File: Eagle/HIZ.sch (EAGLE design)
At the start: 17 parts, among them IC1 IC_UC_PIC12F508SOIC, SW1 SW_TACT_2P-3X6, SW2 SW_SLIDE

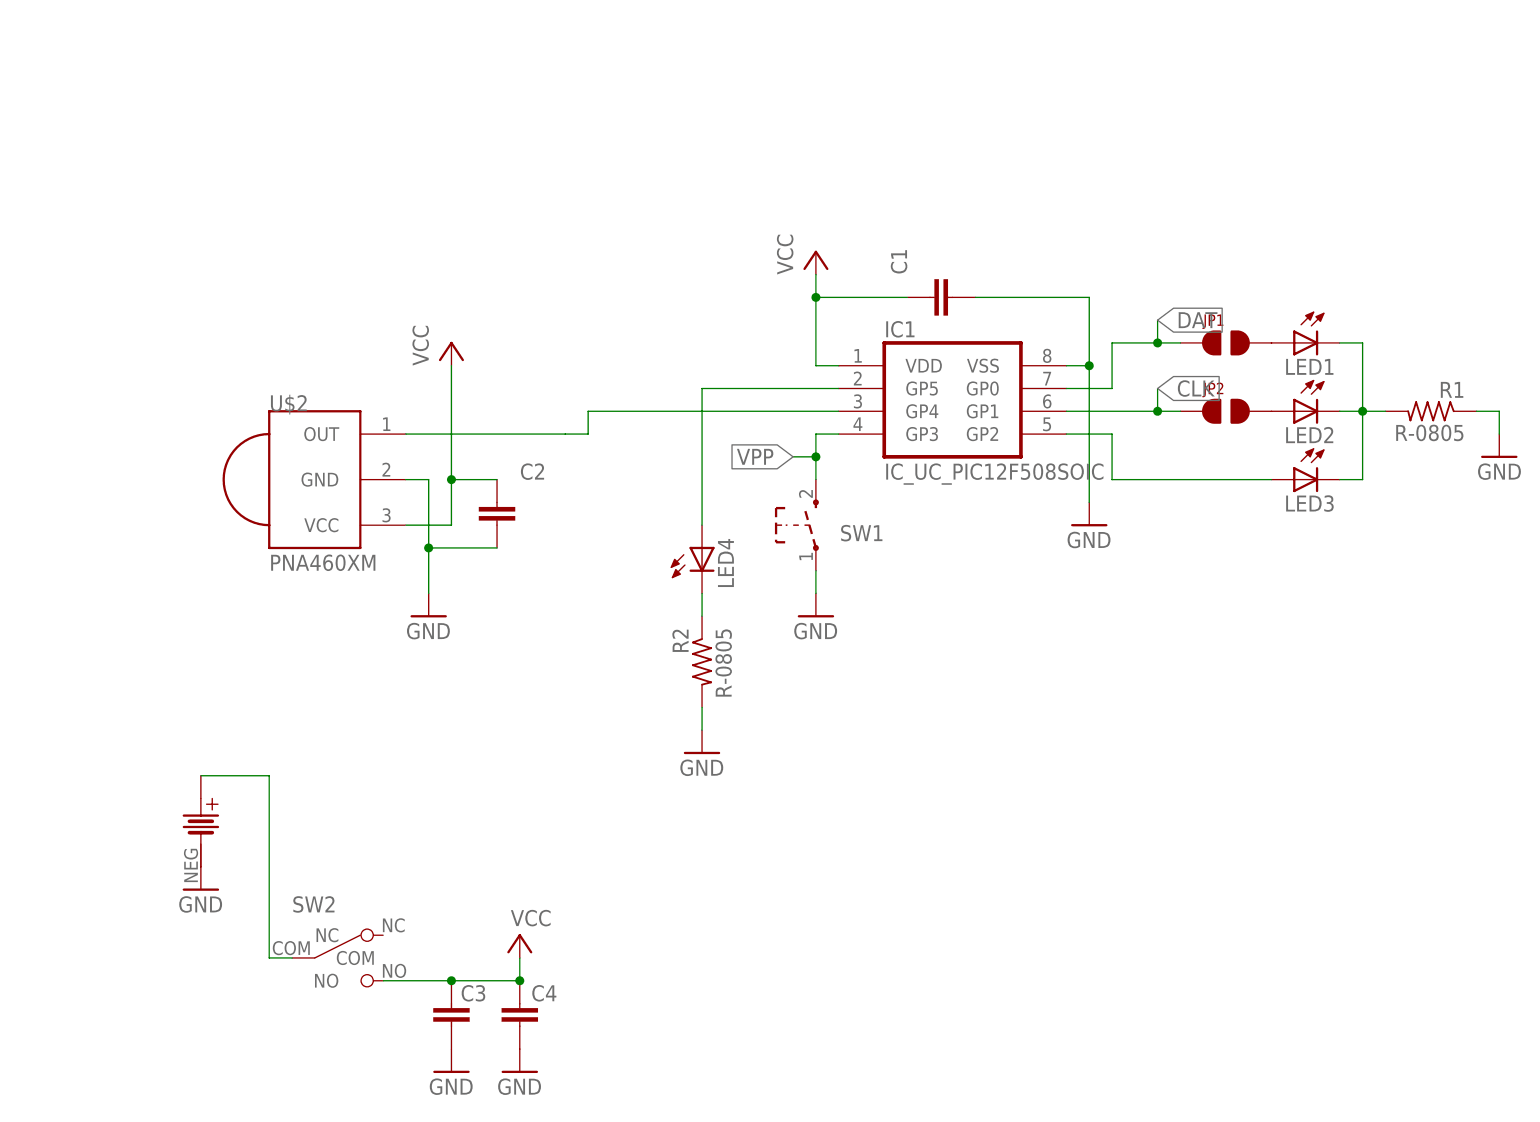
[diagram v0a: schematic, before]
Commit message: Added Frame to schematics
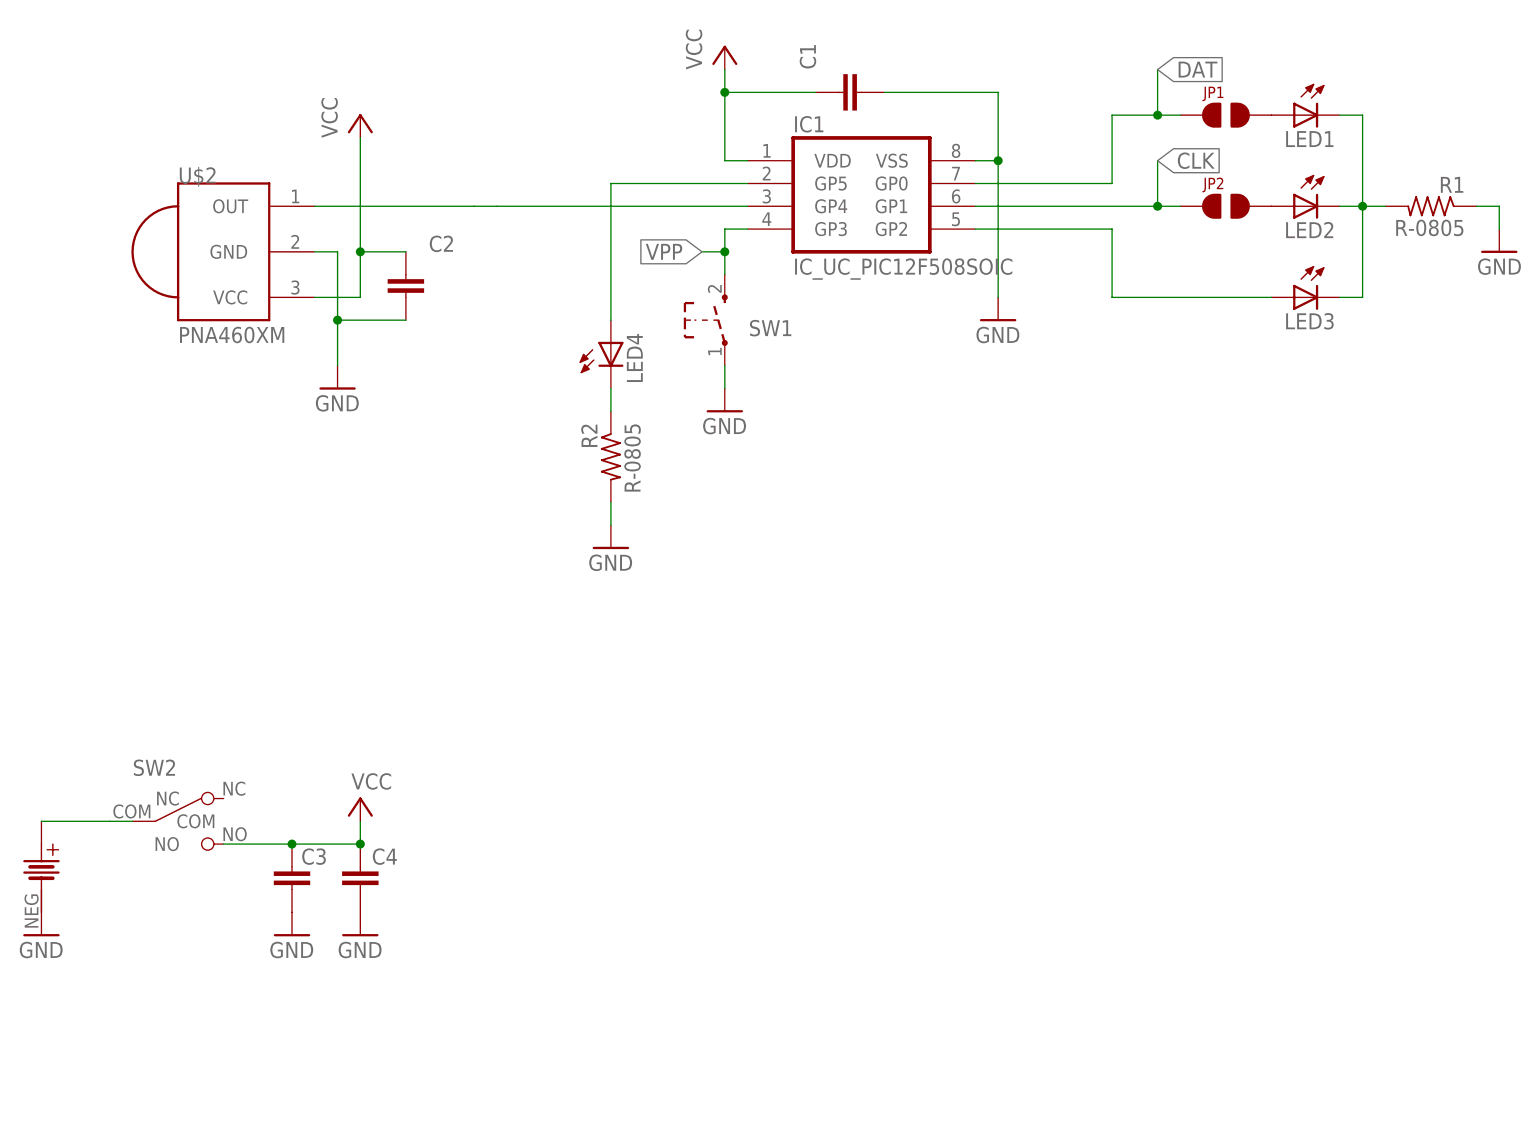
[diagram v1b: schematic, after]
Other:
- moved on the sheet: C1, C2, C3, C4, IC1, JP1, JP2, LED1, LED2, LED3, LED4, R1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

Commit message: Updated info in Frame, added part values.
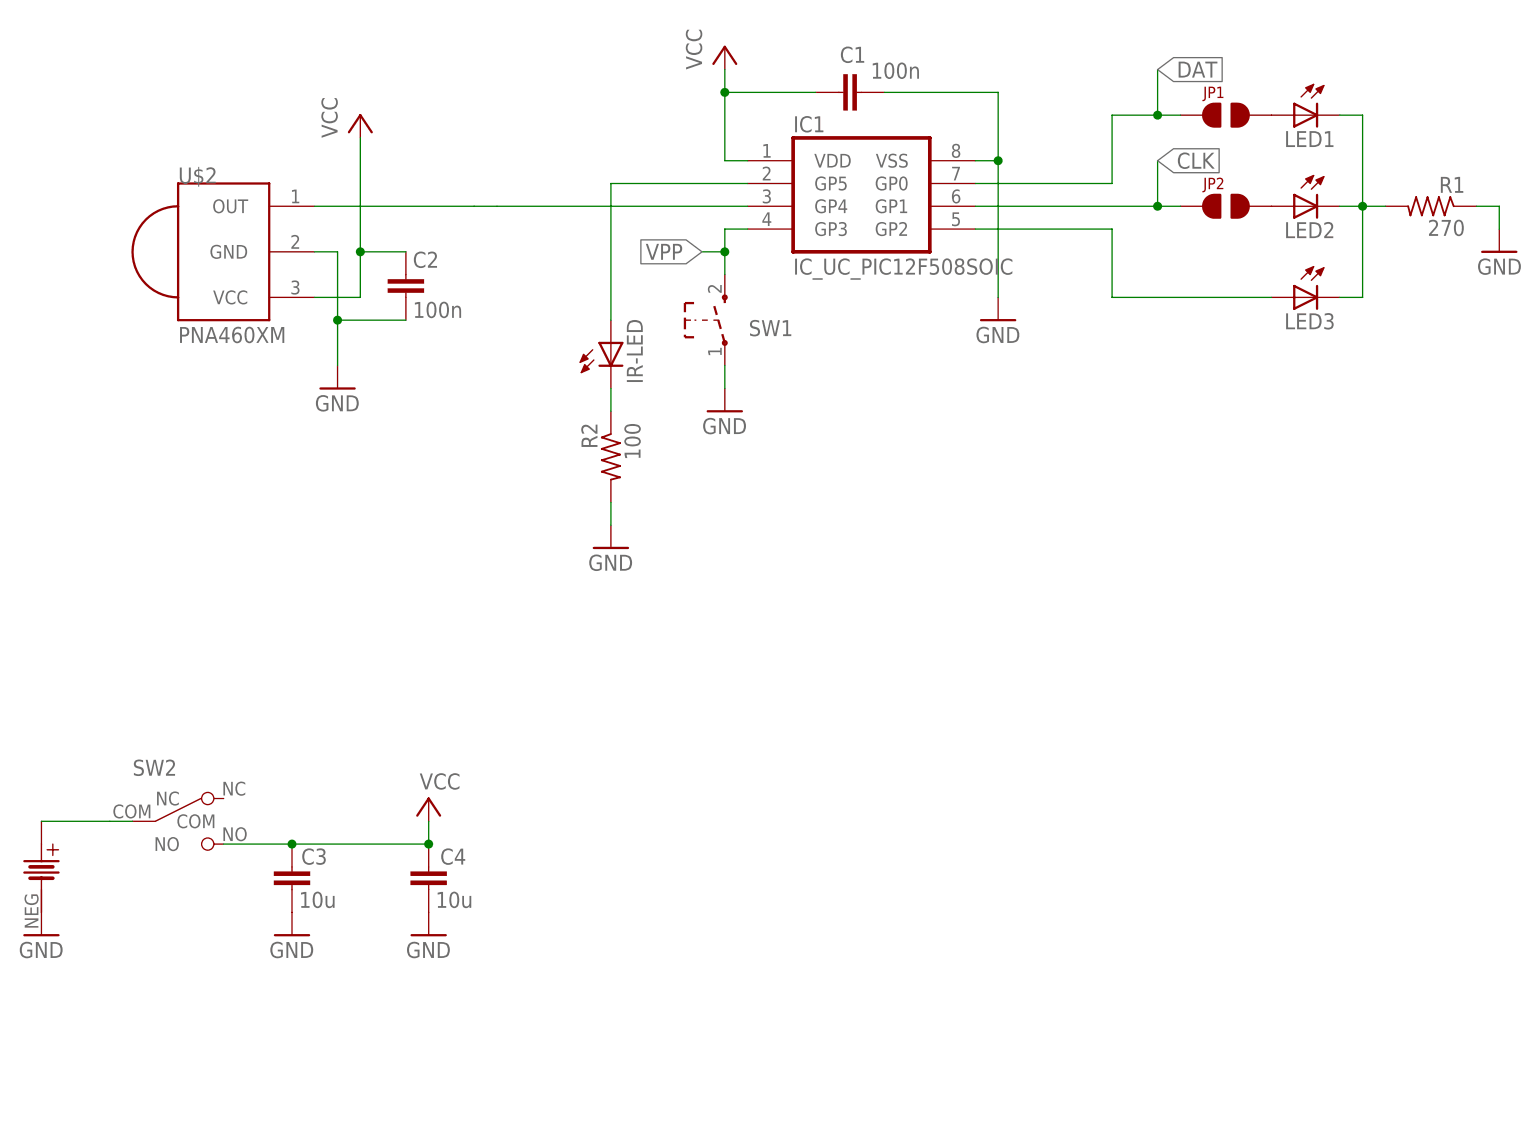
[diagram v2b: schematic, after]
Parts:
- C1, C2: value (none) -> 100n
- C3, C4: value (none) -> 10u
- R1: value R-0805 -> 270
- R2: value R-0805 -> 100
- renumbered LED4 to IR-LED
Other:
- moved on the sheet: C4
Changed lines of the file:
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@@
 <part name="LED2" library="dp_devices" deviceset="LED" device="-0805"/>
 <part name="LED3" library="dp_devices" deviceset="LED" device="-0805"/>
-<part name="LED4" library="adafruit" deviceset="LED" device="SMT1206"/>
+<part name="IR-LED" library="adafruit" deviceset="LED" device="SMT1206"/>
 <part name="SW1" library="dp_devices" deviceset="SW_TACT_2P" device="-3X6"/>
 <part name="IC1" library="dp_devices" deviceset="IC_UC_PIC12F508" device="SOIC"/>
-<part name="R1" library="SmallRoomLabs_Discrete" deviceset="R" device="-0805"/>
+<part name="R1" library="SmallRoomLabs_Discrete" deviceset="R" device="-0805" value="270"/>
 <part name="GND1" library="supply1" deviceset="GND" device=""/>
 <part name="GND3" library="supply1" deviceset="GND" device=""/>
@@
 <part name="SW2" library="dp_devices" deviceset="SW_SLIDE" device=""/>
 <part name="GND4" library="supply1" deviceset="GND" device=""/>
-<part name="C1" library="dp_devices" deviceset="CAPACITOR_NPOL" device="-0805"/>
-<part name="C2" library="dp_devices" deviceset="CAPACITOR_NPOL" device="-0805"/>
+<part name="C1" library="dp_devices" deviceset="CAPACITOR_NPOL" device="-0805" value="100n"/>
+<part name="C2" library="dp_devices" deviceset="CAPACITOR_NPOL" device="-0805" value="100n"/>
 <part name="GND5" library="supply1" deviceset="GND" device=""/>
-<part name="C3" library="dp_devices" deviceset="CAPACITOR_NPOL" device="-0805"/>
-<part name="C4" library="dp_devices" deviceset="CAPACITOR_NPOL" device="-0805"/>
+<part name="C3" library="dp_devices" deviceset="CAPACITOR_NPOL" device="-0805" value="10u"/>
+<part name="C4" library="dp_devices" deviceset="CAPACITOR_NPOL" device="-0805" value="10u"/>
 <part name="GND6" library="supply1" deviceset="GND" device=""/>
 <part name="GND7" library="supply1" deviceset="GND" device=""/>
-<part name="R2" library="SmallRoomLabs_Discrete" deviceset="R" device="-0805"/>
+<part name="R2" library="SmallRoomLabs_Discrete" deviceset="R" device="-0805" value="100"/>
 <part name="GND8" library="supply1" deviceset="GND" device=""/>
 <part name="JP1" library="SmallRoomLabs_ConSwitch" deviceset="JP2" device="-TINY"/>
@@
 <part name="BA1" library="SmallRoomLabs_Battery" deviceset="BATTERY-3V" device="2032PTH-CHEAP"/>
 <part name="GND9" library="supply1" deviceset="GND" device=""/>
-<part name="U$1" library="SmallRoomLabs" deviceset="FRAME" device=""/>
+<part name="U$1" library="SmallRoomLabs_Misc" deviceset="FRAME" device="" value="0.1"/>
 </parts>
 <sheets>
@@
 <instance part="LED2" gate="LED" x="157.48" y="99.06" rot="MR270"/>
 <instance part="LED3" gate="LED" x="157.48" y="88.9" rot="MR270"/>
-<instance part="LED4" gate="G$1" x="81.28" y="83.82"/>
+<instance part="IR-LED" gate="G$1" x="81.28" y="83.82"/>
 <instance part="SW1" gate="SW" x="93.98" y="86.36" smashed="yes" rot="R90">
 <attribute name="NAME" x="101.6" y="86.36" size="1.778" layer="95" font="vector" rot="R180"/>
@@
 <instance part="GND3" gate="1" x="50.8" y="78.74"/>
 <instance part="P+1" gate="VCC" x="53.34" y="109.22"/>
-<instance part="P+2" gate="VCC" x="53.34" y="33.02" smashed="yes">
-<attribute name="VALUE" x="56.896" y="35.814" size="1.778" layer="96" rot="R180"/>
+<instance part="P+2" gate="VCC" x="60.96" y="33.02" smashed="yes">
+<attribute name="VALUE" x="64.516" y="35.814" size="1.778" layer="96" rot="R180"/>
 </instance>
 <instance part="P+3" gate="VCC" x="93.98" y="116.84"/>
@@
 </instance>
 <instance part="GND4" gate="1" x="124.46" y="86.36"/>
-<instance part="C1" gate="C" x="109.22" y="111.76" rot="R90"/>
-<instance part="C2" gate="C" x="58.42" y="88.9"/>
+<instance part="C1" gate="C" x="109.22" y="111.76" smashed="yes" rot="R90">
+<attribute name="NAME" x="109.728" y="116.84" size="1.778" layer="95" rot="R180"/>
+<attribute name="VALUE" x="110.236" y="113.284" size="1.778" layer="96"/>
+</instance>
+<instance part="C2" gate="C" x="58.42" y="88.9" smashed="yes">
+<attribute name="NAME" x="59.182" y="92.202" size="1.778" layer="95"/>
+<attribute name="VALUE" x="59.182" y="86.614" size="1.778" layer="96"/>
+</instance>
 <instance part="GND5" gate="1" x="93.98" y="76.2"/>
 <instance part="C3" gate="C" x="45.72" y="22.86" smashed="yes">
 <attribute name="NAME" x="46.736" y="25.654" size="1.778" layer="95"/>
-<attribute name="VALUE" x="48.26" y="25.4" size="1.778" layer="96"/>
-</instance>
-<instance part="C4" gate="C" x="53.34" y="22.86" smashed="yes">
-<attribute name="NAME" x="54.61" y="25.654" size="1.778" layer="95"/>
-<attribute name="VALUE" x="55.88" y="25.4" size="1.778" layer="96"/>
+<attribute name="VALUE" x="46.482" y="20.828" size="1.778" layer="96"/>
+</instance>
+<instance part="C4" gate="C" x="60.96" y="22.86" smashed="yes">
+<attribute name="NAME" x="62.23" y="25.654" size="1.778" layer="95"/>
+<attribute name="VALUE" x="61.722" y="20.828" size="1.778" layer="96"/>
 </instance>
 <instance part="GND6" gate="1" x="45.72" y="17.78"/>
-<instance part="GND7" gate="1" x="53.34" y="17.78"/>
+<instance part="GND7" gate="1" x="60.96" y="17.78"/>
 <instance part="R2" gate="R" x="81.28" y="71.12" rot="MR270"/>
 <instance part="GND8" gate="1" x="81.28" y="60.96"/>
@@
 <pinref part="P+2" gate="VCC" pin="VCC"/>
 <pinref part="C3" gate="C" pin="1"/>
-<wire x1="45.72" y1="27.94" x2="53.34" y2="27.94" width="0.1524" layer="91"/>
+<wire x1="45.72" y1="27.94" x2="60.96" y2="27.94" width="0.1524" layer="91"/>
 <junction x="45.72" y="27.94"/>
 <pinref part="C4" gate="C" pin="1"/>
-<wire x1="53.34" y1="27.94" x2="53.34" y2="30.48" width="0.1524" layer="91"/>
-<junction x="53.34" y="27.94"/>
+<wire x1="60.96" y1="27.94" x2="60.96" y2="30.48" width="0.1524" layer="91"/>
+<junction x="60.96" y="27.94"/>
 </segment>
 <segment>
@@
 <segment>
 <pinref part="R2" gate="R" pin="1"/>
-<pinref part="LED4" gate="G$1" pin="C"/>
+<pinref part="IR-LED" gate="G$1" pin="C"/>
 <wire x1="81.28" y1="76.2" x2="81.28" y2="78.74" width="0.1524" layer="91"/>
 </segment>
@@
 <net name="N$8" class="0">
 <segment>
-<pinref part="LED4" gate="G$1" pin="A"/>
+<pinref part="IR-LED" gate="G$1" pin="A"/>
 <wire x1="81.28" y1="86.36" x2="81.28" y2="99.06" width="0.1524" layer="91"/>
 <pinref part="IC1" gate="G$1" pin="GP5"/>
